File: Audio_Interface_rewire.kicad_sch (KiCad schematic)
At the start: 62 parts, among them IC1 REG103GA-3.3_2K5, IC2 PCM2906CDB, IC3 INA849DGKT, J1 USB_B_Micro, J2 SJ-435107RS, J3 Vol. knob1 22k, J4 Vol. knob2 22k, J5 SW_PUSH_3PDT, J6 External mic. conn., Q1 J304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

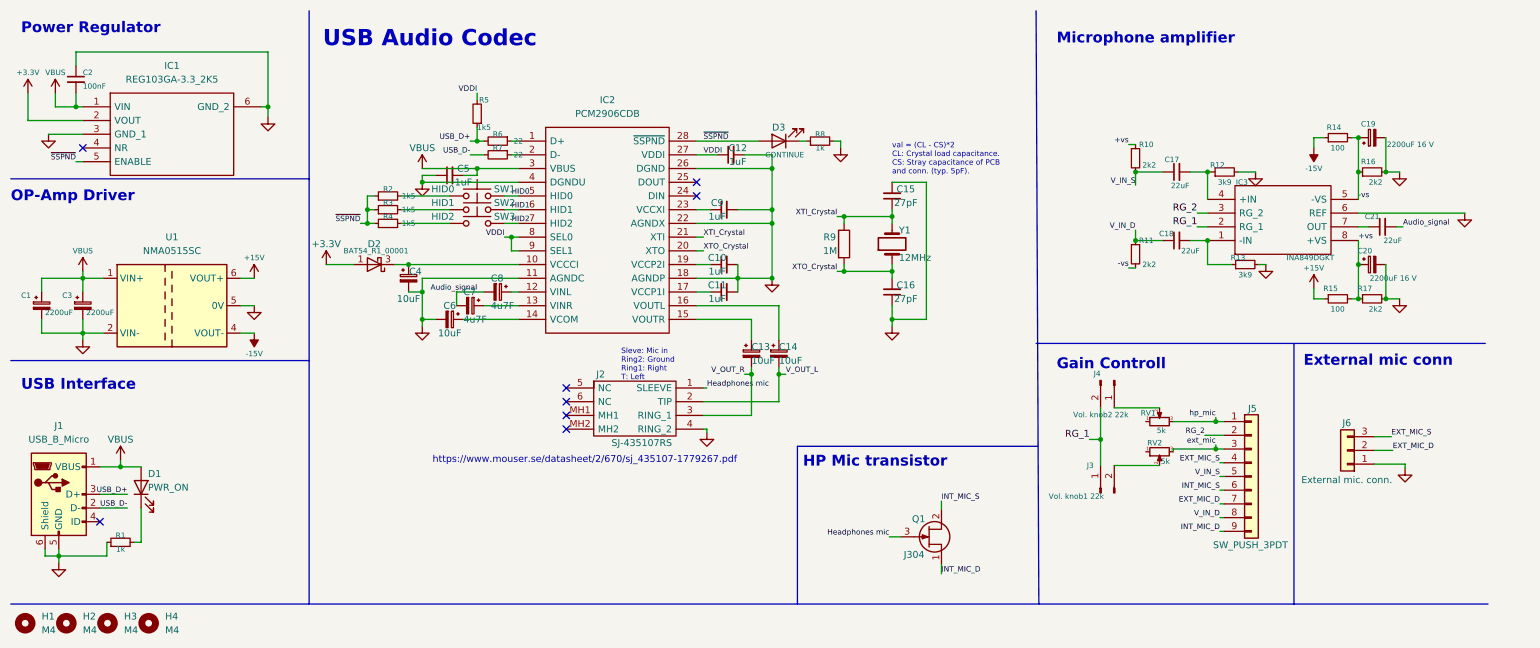
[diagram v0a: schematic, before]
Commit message: New version without consideration for microphone on earbuds
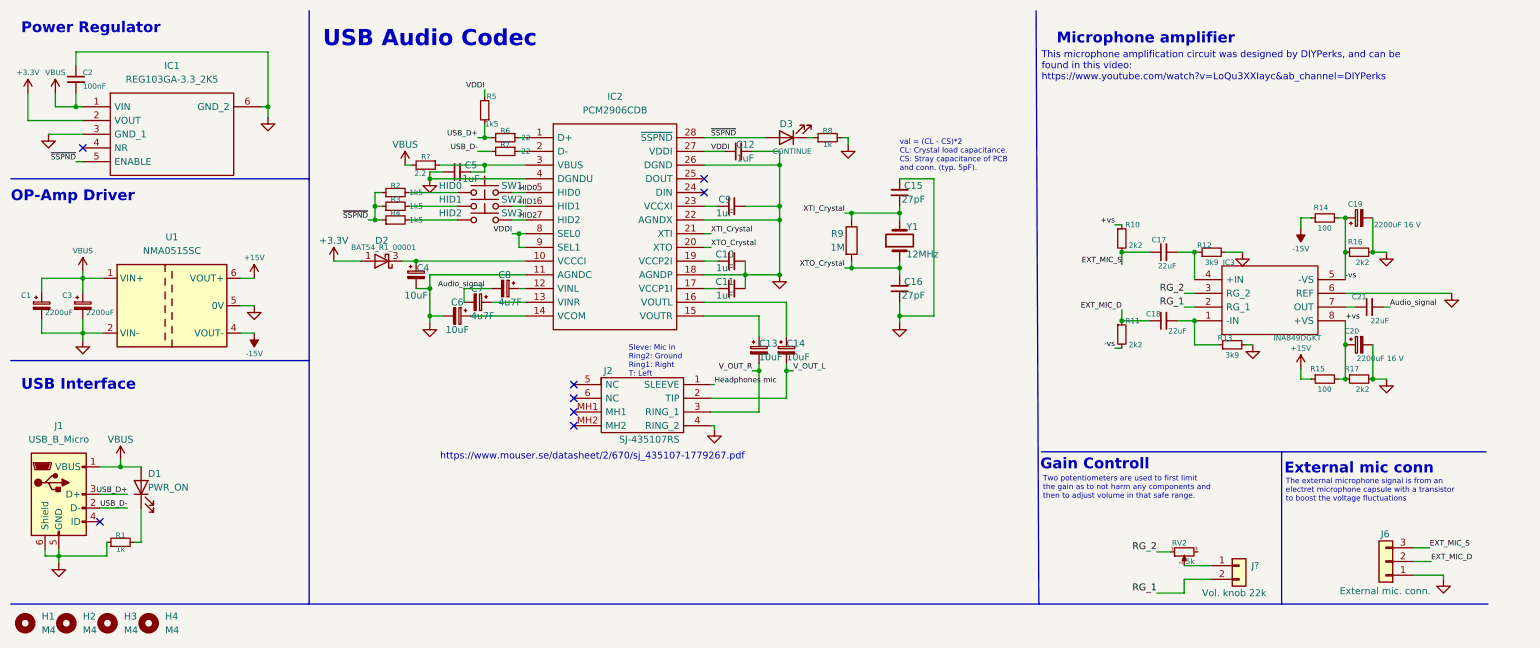
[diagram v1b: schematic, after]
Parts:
- removed J3: Vol. knob1 22k, Connector_JST:JST_XH_B2B-XH-AM_1x02_P2.50mm_Vertical, symbol Connector:Conn_01x02_Male
- removed J4: Vol. knob2 22k, Connector_JST:JST_XH_B2B-XH-AM_1x02_P2.50mm_Vertical, symbol Connector:Conn_01x02_Male
- removed J5: SW_PUSH_3PDT, Connector_JST:JST_XH_B9B-XH-AM_1x09_P2.50mm_Vertical, symbol Connector_Generic:Conn_01x09
- removed Q1: J304, Package_TO_SOT_SMD:SOT-23, symbol Transistor_FET:BF545B
- removed RV1: 5k, IC_Downloaded:3362P_1, symbol Device:R_Potentiometer_Small
- added J?: Vol. knob 22k, symbol Connector_Generic:Conn_01x02
- added R?: 2.2, Resistor_SMD:R_0805_2012Metric_Pad1.20x1.40mm_HandSolder, symbol Device:R_Small
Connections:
- net V_IN_D is gone; now on net EXT_MIC_D: C18.1, R11.1
- net V_IN_S is gone; now on net EXT_MIC_S: C17.1, R10.2
- net RG_1: now also J?.2 (Pin_2)
- net RG_2: now also RV2.1
- net VBUS: now also R?.2; no longer C5.2, IC2.3 (VBUS)
- net at RV2.2: now also J?.1 (Pin_1)
- net ext_mic: no longer names the net of RV2.3
- new net: C5.2, IC2.3 (VBUS), R?.1
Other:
- note added: "The external microphone signal is from an electret microphone capsule with a transistor to boost the voltage fluctuations"
- note added: "This microphone amplification circuit was designed by DIYPerks, and can be found in this video: https://www.youtube.com/watch?v=LoQu3XXIayc&ab_channel=DIYPerks"
- note added: "Two potentiometers are used to first limit the gain as to not harm any components and then to adjust volume in that safe range."
- note removed: "HP Mic transistor"
- moved on the sheet: C10, C11, C12, C13, C14, C15, C16, C17, C18, C19, C20, C21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
